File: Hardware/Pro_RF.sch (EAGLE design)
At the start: 41 parts, among them U1 MCP73831, U2 915MHz, U5 ATmega32U4, U6 3.3V, Y2 8MHz

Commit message: Adding prod IDs. This changed some FPs so fixed routes. Moved Int Pin to avoid I2C
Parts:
- R10, R13, R7, R9: value 330 -> 1k; device SparkFun-Resistors:330OHM-0603-1/10W-1% -> SparkFun-Resistors:1KOHM-0603-1/10W-1%
- S1: value (none) -> Power
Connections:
- removed net D3: U2.DIO0, U5.PD0(SCL)
- removed net D5: J3.8, U5.PC6
- new net RFM_INT: J3.8, U2.DIO0, U5.PC6
- new net SCL: U5.PD0(SCL)
- new net SDA: U5.PD1(SDA)
- net D2: no longer U5.PD1(SDA)
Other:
- note added: "Add Qwiic?"
- note added: "Add status LED"
- note added: "GND holes need silk label below Xtal"
- note added: "Increase hole size for ant strain relief to accept 22 awg wire"
- note added: "LEDs need labels"
- note added: "Panel doesn't depanlize. Add space between RST/power switch. Overhanging USB"
- note added: "Programming header?"
- note added: "RST silk on bottom broken by hole"
- note added: "TX/RX LEDs are always on? Hooked up wrong?"
- moved on the sheet: C12, C13, C14, LED1, R11, R12, R13, U6

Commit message: Many updates. v02.
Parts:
- removed U5: ATmega32U4, SparkFun-IC-Microcontroller:ATMEGA32U4QFN2
- added D2: BLUE, SparkFun-LED:LED-BLUE0603
- added J10: AVR_SPI_PROG_3X2TESTPOINTS, SparkFun-Connectors:AVR_SPI_PROG_3X2TESTPOINTS
- added J11: (no value), SparkFun-Connectors:CONN_09NO_SILK
- added J12: JST, SparkFun-Connectors:CONN_02-JST-2MM-SMT
- added J2: (no value), SparkFun-Connectors:QWIIC_CONNECTORJS-1MM
- added JP2: JUMPER-SMT_2_NO_SILK, SparkFun-Jumpers:JUMPER-SMT_2_NO_SILK
- added R1, R2: 10k, SparkFun-Resistors:10KOHM-0603-1/10W-1%
- added R3: 1k, SparkFun-Resistors:1KOHM-0603-1/10W-1%
- added U$26: SPECIAL_INSTRUCTIONS-ORDERING, SparkFun-Aesthetics:SPECIAL_INSTRUCTIONS-ORDERING
- added U3: 32U4, SparkFun-IC-Microcontroller:ATMEGA32U4-ARDUINOQFN2
- C9: device SparkFun-Capacitors:4.7UF0603 -> SparkFun-Capacitors:4.7UF-0603-6.3V-(10%)
- D1: value GREEN -> Green
- D6: value BLUE -> Yellow; device SparkFun-LED:LED-BLUE0603 -> SparkFun-LED:LED-YELLOW0603
- J4: device SparkFun-Connectors:CONN_10NO_SILK_PTH_FEMALE -> SparkFun-Connectors:CONN_01PTH_NO_SILK_YES_STOP
- J7: value (none) -> PTH
- J9: value (none) -> External On/Off
- JP1: value (none) -> JUMPER-SMT_2_NO_SILK; device SparkFun-Connectors:CONN_02-JST-2MM-SMT -> SparkFun-Jumpers:JUMPER-SMT_2_NO_SILK
- SJ2: device SparkFun:SOLDERJUMPERTRACE -> SparkFun-Jumpers:JUMPER-SMT_2_NC_TRACE_SILK
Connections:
- removed net A5: U5.PF0(ADC0)
- removed net D14: R10.1, U5.PB0(SS)
- removed net D2: J3.10
- removed net D4: J3.9, U5.PD4(ADC8)
- removed net D7: J3.6, U5.PE6
- removed net N$15: D1.A, R7.2
- removed net N$19: D6.A, R10.2
- removed net RST: J4.1, R6.1, S3.1, U5.!RESET
- new net !CS: U2.!CS, U3.A5
- new net !RST: J10.5, J11.1, R6.1, S3.1, U3.!RESET
- new net D5: J3.8, U3.D5#
- new net N$1: D6.C, R10.2
- new net N$2: D1.C, R7.2
- new net N$3: D2.A, R3.1
- new net RFM_IO1: JP1.1, U2.IO1
- new net RFM_IO2: JP2.1, U2.IO2
- new net RXLED: R10.1, U3.RXLED
- new net SHLD: J1.SHIELD
- new net STAT: R3.2, U3.D13#
- net 3.3V: now also D1.A, D6.A, J10.2, J2.2, U2.VCC, U3.AVCC, U3.VCC; no longer U2.3.3V, U5.AVCC@24, U5.AVCC@44, U5.VCC@14, U5.VCC@34
- net A0: now also J11.6, U3.A0; no longer J4.6, U5.PF7(ADC7)
- net A1: now also J11.5, U3.A1; no longer J4.5, U5.PF6(ADC6)
- net A2: now also J11.4, U3.A2; no longer J4.4, U5.PF5(ADC5)
- net A3: now also J11.3, U3.A3; no longer J4.3, U5.PF4(ADC4)
- net A4: now also J11.2, U3.A4; no longer J4.2, U5.PF1(ADC1)
- net ANT: now also J4.1; no longer J4.10
- net AREF: now also U3.AREF; no longer U5.AREF
- net D+: now also U3.D+; no longer U5.D+
- net D-: now also U3.D-; no longer U5.D-
- net D10: now also J3.4, JP1.2, U3.D10#; no longer U2.NSS, U5.PB6(ADC13)
- net D11: now also JP2.2, U3.D11#; no longer U5.PB7
- net D6: now also U3.D6#/A7; no longer U5.PD7(ADC10)
- net D8: now also J3.6, U3.D8; no longer J3.5, U5.PB4(ADC11)
- net D9: now also J3.5, U3.D9#/A8; no longer J3.4, U5.PB5(ADC12)
- net GND: now also D2.C, J10.6, J12.2, J2.1, R2.1, U2.GND, U3.GND, U3.PE2/!HWB, U3.UGND; no longer D1.C, D6.C, JP1.2, U2.GND@1, U2.GND@2, U5.GND@15, U5.GND@23, U5.GND@35, U5.GND@43, U5.PE2/!HWB, U5.UGND
- net MISO: now also J10.1, J11.7, U3.D14/MISO; no longer J4.7, U5.PB3(MISO)
- net MOSI: now also J10.4, J11.8, U3.D16/MOSI; no longer J4.8, U5.PB2(MOSI)
- net N$16: now also U3.XTAL2; no longer U5.XTAL2
- net N$17: now also U3.XTAL1; no longer U5.XTAL1
- net RFM_INT: now also U2.IO0/INT, U3.D7; no longer J3.8, U2.DIO0, U5.PC6
- net RFM_RST: now also U2.RST, U3.D4/A6; no longer U2.RESET, U5.PC7
- net RXI: now also J3.10, U3.D0(RX); no longer U5.PD2(RX)
- net SCK: now also J10.3, J11.9, U3.D15/SCK; no longer J4.9, U5.PB1(SCK)
- net SCL: now also J2.4, U3.D3#(SCL); no longer U5.PD0(SCL)
- net SDA: now also J2.3, U3.D2(SDA); no longer U5.PD1(SDA)
- net TXLED: now also U3.TXLED; no longer U5.PD5
- net TXO: now also J3.9, U3.D1(TX); no longer U5.PD3(TX)
- net UCAP: now also U3.UCAP; no longer U5.UCAP
- net USB_VCC: now also U3.UVCC, U3.VBUS; no longer U5.UVCC, U5.VBUS
- net VBATT: now also J12.1, R1.2; no longer JP1.1
- net VBATT_LVL: now also R1.1, R2.2, U3.D12/A10; no longer U5.PD6(ADC9)
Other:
- note added: "500mA charging"
- note added: "Close jumpers for LoRa WAN compatibility"
- note added: "Max Current Output: 600mA"
- note added: "Max Voltage Input: 6VDC"
- note removed: "10K for 100mA charging"
- note removed: "2K for 500mA charging"
- note removed: "Add Qwiic?"
- note removed: "Add status LED"
- note removed: "GND holes need silk label below Xtal"
- note removed: "Increase hole size for ant strain relief to accept 22 awg wire"
- note removed: "LEDs need labels"
- note removed: "Max Current Output: 500mA"
- note removed: "Max Voltage Input: 16VDC"
- note removed: "Panel doesn't depanlize. Add space between RST/power switch. Overhanging USB"
- note removed: "Programming header?"
- note removed: "RST silk on bottom broken by hole"
- note removed: "TX/RX LEDs are always on? Hooked up wrong?"
- moved on the sheet: C12, C13, C14, D1, D6, F1, J7, J9, LED1, R10, R11, R12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

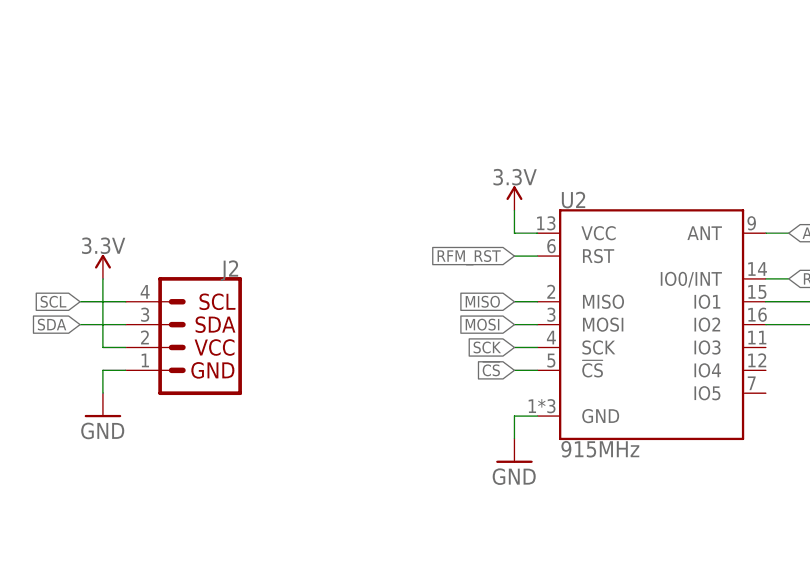
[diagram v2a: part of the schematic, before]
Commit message: Adding pullup to CS
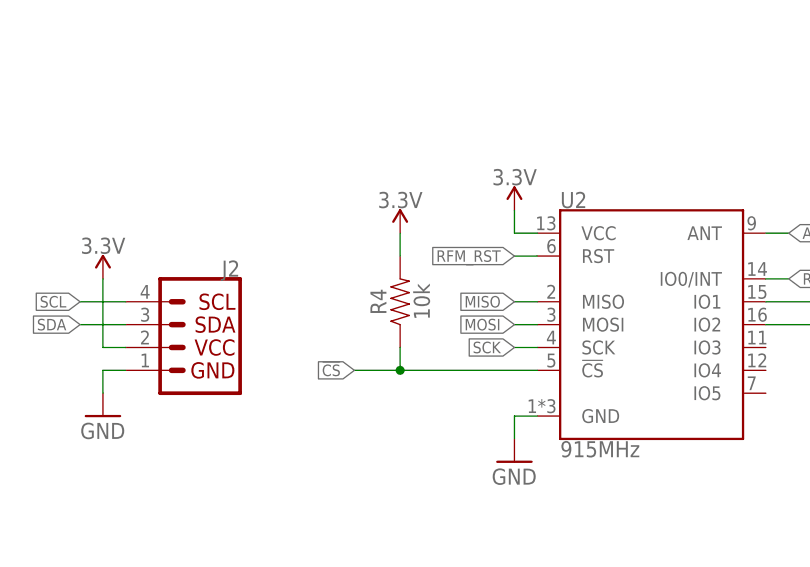
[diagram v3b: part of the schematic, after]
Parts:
- added R4: 10k, SparkFun-Resistors:10KOHM-0603-1/10W-1%
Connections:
- net !CS: now also R4.1
- net 3.3V: now also R4.2
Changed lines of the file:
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@@
 <part name="JP2" library="SparkFun-Jumpers" deviceset="JUMPER-SMT_2_NO" device="_SILK" value=""/>
 <part name="U$26" library="SparkFun-Aesthetics" deviceset="SPECIAL_INSTRUCTIONS" device="-ORDERING"/>
+<part name="R4" library="SparkFun-Resistors" deviceset="10KOHM" device="-0603-1/10W-1%" value="10k"/>
+<part name="P+7" library="SparkFun-PowerSymbols" deviceset="3.3V" device=""/>
 </parts>
 <sheets>
@@
 </instance>
 <instance part="U$26" gate="G$1" x="375.92" y="17.78"/>
+<instance part="R4" gate="G$1" x="327.66" y="104.14" rot="R90"/>
+<instance part="P+7" gate="G$1" x="327.66" y="111.76"/>
 </instances>
 <busses>
@@
 <wire x1="378.46" y1="269.24" x2="378.46" y2="266.7" width="0.1524" layer="91"/>
 </segment>
+<segment>
+<pinref part="R4" gate="G$1" pin="2"/>
+<pinref part="P+7" gate="G$1" pin="3.3V"/>
+<wire x1="327.66" y1="111.76" x2="327.66" y2="109.22" width="0.1524" layer="91"/>
+</segment>
 </net>
 <net name="N$5" class="0">
@@
 <net name="!CS" class="0">
 <segment>
-<wire x1="342.9" y1="96.52" x2="340.36" y2="96.52" width="0.1524" layer="91"/>
-<label x="340.36" y="96.52" size="1.27" layer="95" rot="R180" xref="yes"/>
+<wire x1="342.9" y1="96.52" x2="327.66" y2="96.52" width="0.1524" layer="91"/>
+<label x="322.58" y="96.52" size="1.27" layer="95" rot="R180" xref="yes"/>
 <pinref part="U2" gate="U1" pin="!CS"/>
-</segment>
-<segment>
+<pinref part="R4" gate="G$1" pin="1"/>
+<wire x1="327.66" y1="96.52" x2="322.58" y2="96.52" width="0.1524" layer="91"/>
+<wire x1="327.66" y1="99.06" x2="327.66" y2="96.52" width="0.1524" layer="91"/>
+<junction x="327.66" y="96.52"/>
+</segment>
+<segment>

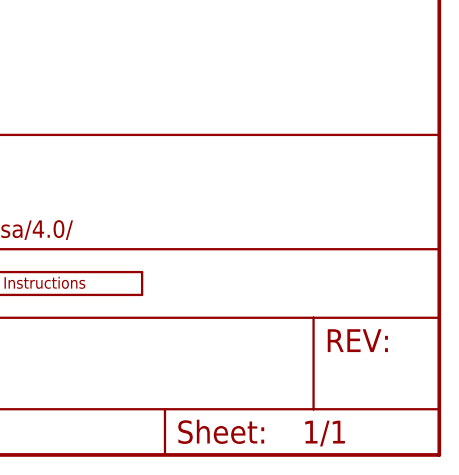
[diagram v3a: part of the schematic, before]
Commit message: Adding Examples
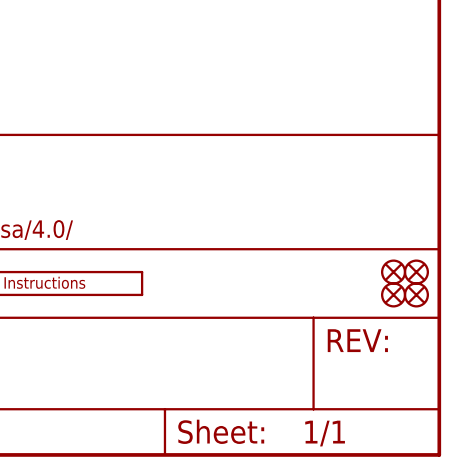
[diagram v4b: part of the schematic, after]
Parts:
- added FD1, FD2, FD3, FD4: FIDUCIAL1X2, SparkFun-Aesthetics:FIDUCIAL1X2
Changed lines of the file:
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@@
 <part name="P+4" library="SparkFun-PowerSymbols" deviceset="3.3V" device=""/>
 <part name="C9" library="SparkFun-Capacitors" deviceset="4.7UF" device="-0603-6.3V-(10%)" value="4.7uF"/>
-<part name="GND18" library="supply1" deviceset="GND" device=""/>
-<part name="GND20" library="supply1" deviceset="GND" device=""/>
+<part name="GND18" library="supply1" library_urn="urn:adsk.eagle:library:371" deviceset="GND" device=""/>
+<part name="GND20" library="supply1" library_urn="urn:adsk.eagle:library:371" deviceset="GND" device=""/>
 <part name="D4" library="SparkFun-LED" deviceset="LED-YELLOW" device="0603" value="Yellow"/>
 <part name="R9" library="SparkFun-Resistors" deviceset="1KOHM" device="-0603-1/10W-1%" value="1k"/>
 <part name="F1" library="SparkFun-Fuses" deviceset="PPTC" device="_HALF-AMP" value="6V/0.5A"/>
-<part name="GND3" library="supply1" deviceset="GND" device=""/>
-<part name="GND4" library="supply1" deviceset="GND" device=""/>
-<part name="GND10" library="supply1" deviceset="GND" device=""/>
+<part name="GND3" library="supply1" library_urn="urn:adsk.eagle:library:371" deviceset="GND" device=""/>
+<part name="GND4" library="supply1" library_urn="urn:adsk.eagle:library:371" deviceset="GND" device=""/>
+<part name="GND10" library="supply1" library_urn="urn:adsk.eagle:library:371" deviceset="GND" device=""/>
 <part name="U1" library="SparkFun-IC-Power" deviceset="MCP73831" device=""/>
 <part name="R5" library="SparkFun-Resistors" deviceset="2.0KOHM" device="-0603-1/10W-5%" value="2.0k"/>
-<part name="GND14" library="supply1" deviceset="GND" device=""/>
-<part name="GND17" library="supply1" deviceset="GND" device=""/>
+<part name="GND14" library="supply1" library_urn="urn:adsk.eagle:library:371" deviceset="GND" device=""/>
+<part name="GND17" library="supply1" library_urn="urn:adsk.eagle:library:371" deviceset="GND" device=""/>
 <part name="C12" library="SparkFun-Capacitors" deviceset="1.0UF" device="-0603-16V-10%" value="1.0uF"/>
 <part name="C13" library="SparkFun-Capacitors" deviceset="10UF-POLAR" device="-EIA3216-16V-10%(TANT)" value="10uF"/>
@@
 <part name="J1" library="SparkFun-Connectors" deviceset="USB_MICRO-B" device="_HALF_PTH_MILL"/>
 <part name="P+1" library="SparkFun-PowerSymbols" deviceset="3.3V" device=""/>
-<part name="GND2" library="supply1" deviceset="GND" device=""/>
+<part name="GND2" library="supply1" library_urn="urn:adsk.eagle:library:371" deviceset="GND" device=""/>
 <part name="S1" library="SparkFun-Switches" deviceset="SWITCH-SPDT" device="-SMD-RIGHT-ANGLE" value="Power"/>
-<part name="GND6" library="supply1" deviceset="GND" device=""/>
-<part name="GND7" library="supply1" deviceset="GND" device=""/>
+<part name="GND6" library="supply1" library_urn="urn:adsk.eagle:library:371" deviceset="GND" device=""/>
+<part name="GND7" library="supply1" library_urn="urn:adsk.eagle:library:371" deviceset="GND" device=""/>
 <part name="D1" library="SparkFun-LED" deviceset="LED-GREEN" device="0603" value="Green"/>
 <part name="J7" library="SparkFun-Connectors" deviceset="CONN_02" device="1X02_NO_SILK" value="PTH"/>
@@
 <part name="J2" library="SparkFun-Connectors" deviceset="QWIIC_CONNECTOR" device="JS-1MM"/>
 <part name="P+2" library="SparkFun-PowerSymbols" deviceset="3.3V" device=""/>
-<part name="GND1" library="supply1" deviceset="GND" device=""/>
+<part name="GND1" library="supply1" library_urn="urn:adsk.eagle:library:371" deviceset="GND" device=""/>
 <part name="J10" library="SparkFun-Connectors" deviceset="AVR_SPI_PROG_3X2" device="TESTPOINTS"/>
 <part name="GND8" library="SparkFun" deviceset="GND" device=""/>
@@
 <part name="R4" library="SparkFun-Resistors" deviceset="10KOHM" device="-0603-1/10W-1%" value="10k"/>
 <part name="P+7" library="SparkFun-PowerSymbols" deviceset="3.3V" device=""/>
+<part name="FD1" library="SparkFun-Aesthetics" deviceset="FIDUCIAL" device="1X2"/>
+<part name="FD2" library="SparkFun-Aesthetics" deviceset="FIDUCIAL" device="1X2"/>
+<part name="FD3" library="SparkFun-Aesthetics" deviceset="FIDUCIAL" device="1X2"/>
+<part name="FD4" library="SparkFun-Aesthetics" deviceset="FIDUCIAL" device="1X2"/>
 </parts>
 <sheets>
@@
 <instance part="R4" gate="G$1" x="327.66" y="104.14" rot="R90"/>
 <instance part="P+7" gate="G$1" x="327.66" y="111.76"/>
+<instance part="FD1" gate="G$1" x="429.26" y="20.32"/>
+<instance part="FD2" gate="G$1" x="426.72" y="20.32"/>
+<instance part="FD3" gate="G$1" x="426.72" y="17.78"/>
+<instance part="FD4" gate="G$1" x="429.26" y="17.78"/>
 </instances>
 <busses>
@@
 which will not be processed correctly with this version.
 </note>
+<note version="8.2" severity="warning">
+Since Version 8.2, EAGLE supports online libraries. The ids
+of those online libraries will not be understood (or retained)
+with this version.
+</note>
+<note version="8.3" severity="warning">
+Since Version 8.3, EAGLE supports URNs for individual library
+assets (packages, symbols, and devices). The URNs of those assets
+will not be understood (or retained) with this version.
+</note>
 </compatibility>

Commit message: updating to sparkfun silk
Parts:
- added LOGO1: REVISION, SparkFun-Aesthetics:REVISION
- added LOGO2: SFE_LOGO_NAME.1_INCH, SparkFun-Aesthetics:SFE_LOGO_NAME.1_INCH
- added LOGO3: SFE_LOGO_NAME_FLAME.1_INCH, SparkFun-Aesthetics:SFE_LOGO_NAME_FLAME.1_INCH
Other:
- note added: "Andy England"
- note added: "Battery Charging"
- note added: "Connections"
- note added: "Elias Santistevan"
- note added: "Power In"
- note added: "Pro Micro"
- note added: "RFM69HCW Module"
- note added: "USB"
- note added: "v01"
- moved on the sheet: C1, C11, C12, C13, C14, C4, C5, C7, C8, C9, D1, D2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

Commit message: Clean up
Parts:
- added J13: U.FL, SparkFun-Connectors:U.FL
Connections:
- net ANT: now also J13.SIGNAL
- net GND: now also J13.GND@0, J13.GND@1
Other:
- note added: "Antennae"
- note added: "v10"
- note removed: "v01"
- moved on the sheet: C5, C7, J10, J4, R11, R12
